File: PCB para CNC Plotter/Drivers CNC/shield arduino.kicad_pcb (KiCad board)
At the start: 2 copper layers, 75.2 x 80.2 mm, 54 parts, among them J18 Drivers VCC, J19 MXF, J6 MX

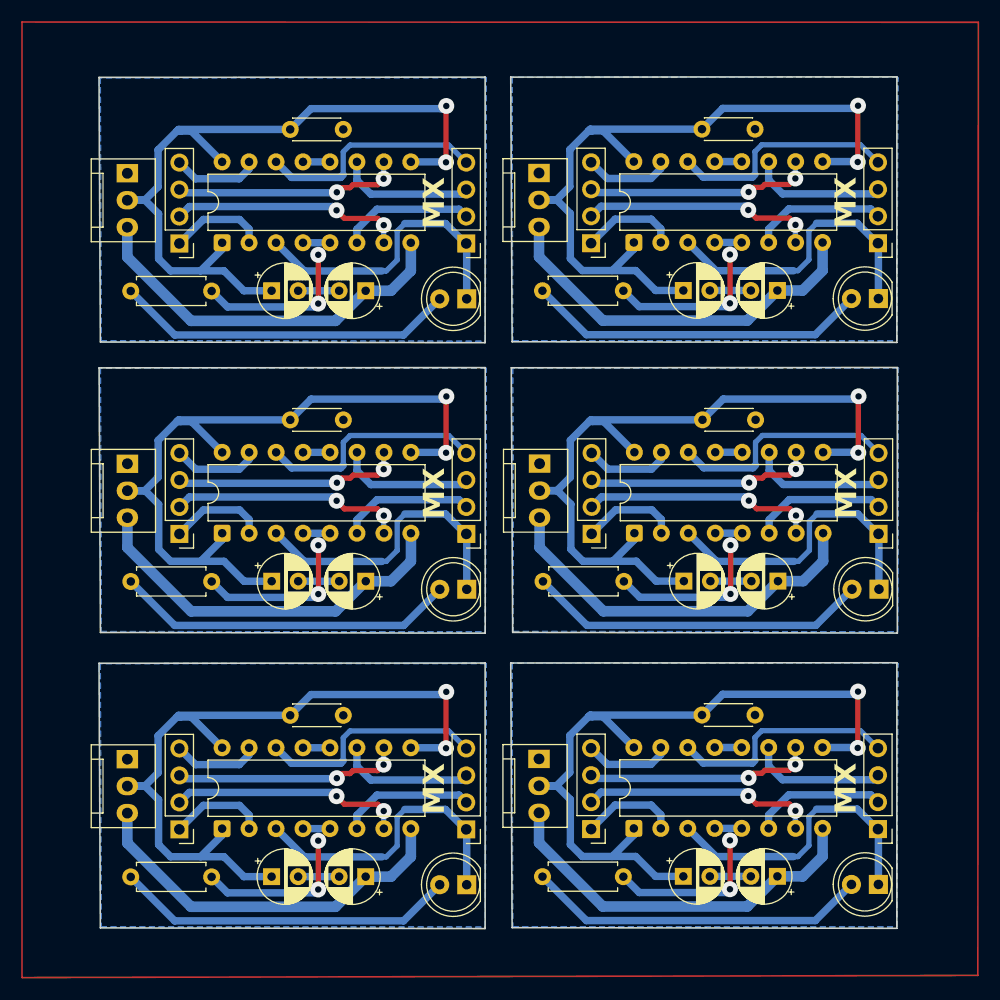
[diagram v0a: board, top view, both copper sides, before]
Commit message: Removido arquivos Gerbers antigos
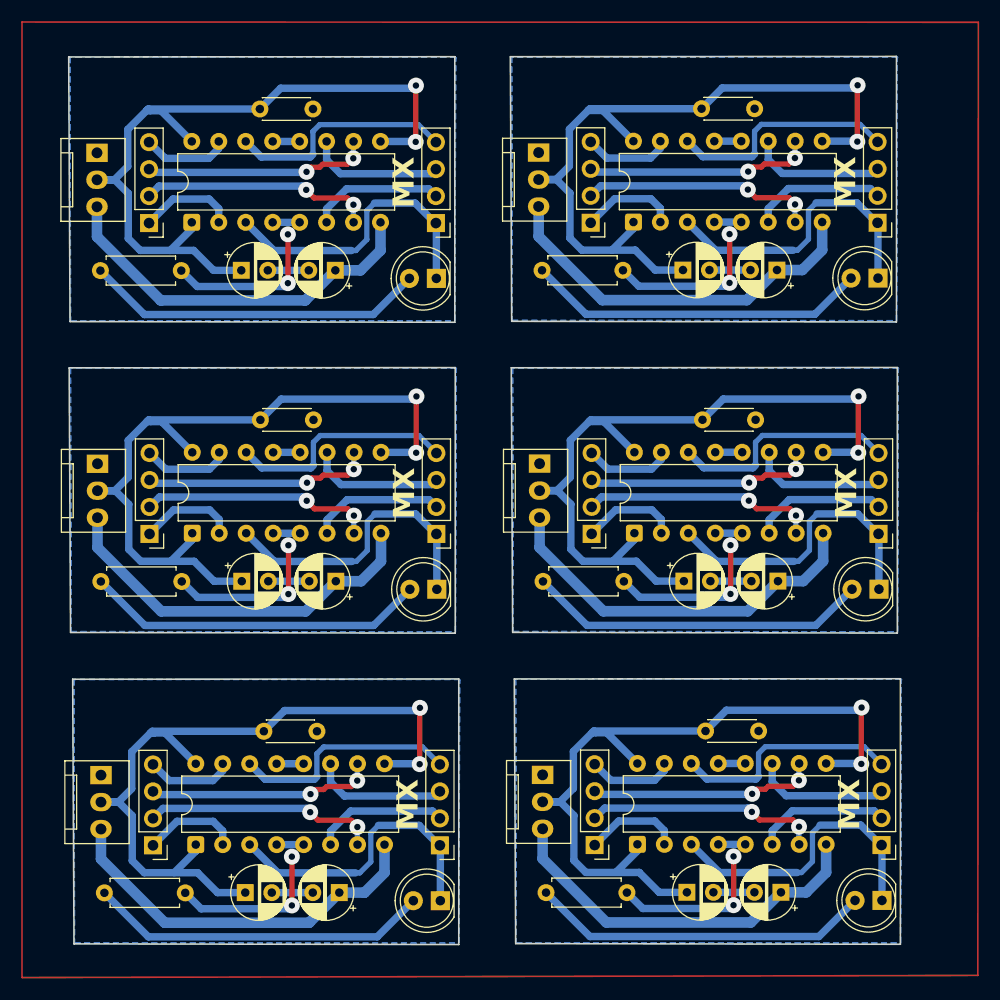
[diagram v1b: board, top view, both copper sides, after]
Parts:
- moved R1 3.44 mm to (126.9, 62.6)
- moved C10 3.44 mm to (132.5, 62.6)
- moved C15 3.44 mm to (141.4, 62.6)
- moved J19 3.44 mm to (123.8, 58.1)
- moved C1 3.44 mm to (139.3, 47.4)
- moved D1 3.44 mm to (150.9, 63.4)
- moved J18 3.44 mm to (118.9, 51.5)
- moved J6 3.44 mm to (150.9, 58.1)
- moved UX1 3.44 mm to (127.9, 58.1)
- moved C10 2.90 mm to (132.9, 121.2)
- moved C15 2.90 mm to (141.8, 121.2)
- moved R1 2.90 mm to (127.2, 121.2)
- moved J18 2.90 mm to (119.3, 110.2)
- moved J19 2.90 mm to (124.2, 116.8)
- moved C1 2.90 mm to (139.7, 106.0)
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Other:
- board size 75.2 x 80.2 mm -> 78.4 x 83.7 mm
